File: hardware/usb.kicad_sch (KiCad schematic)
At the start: 35 parts, among them J1 USB_A_Stacked, J2 USB_C_Receptacle_USB2.0_14P, J3 USB_C_Receptacle_USB2.0_14P, J4 USB_C_Receptacle_USB2.0_14P, U10 SY6280AAC, U11 SY6280AAC, U12 SY6280AAC, U13 TPD2EUSB30, U14 TPD2EUSB30, U15 TPD2EUSB30, U16 TPD2EUSB30, U17 HUSB237, U18 TPD2EUSB30, U9 SY6280AAC

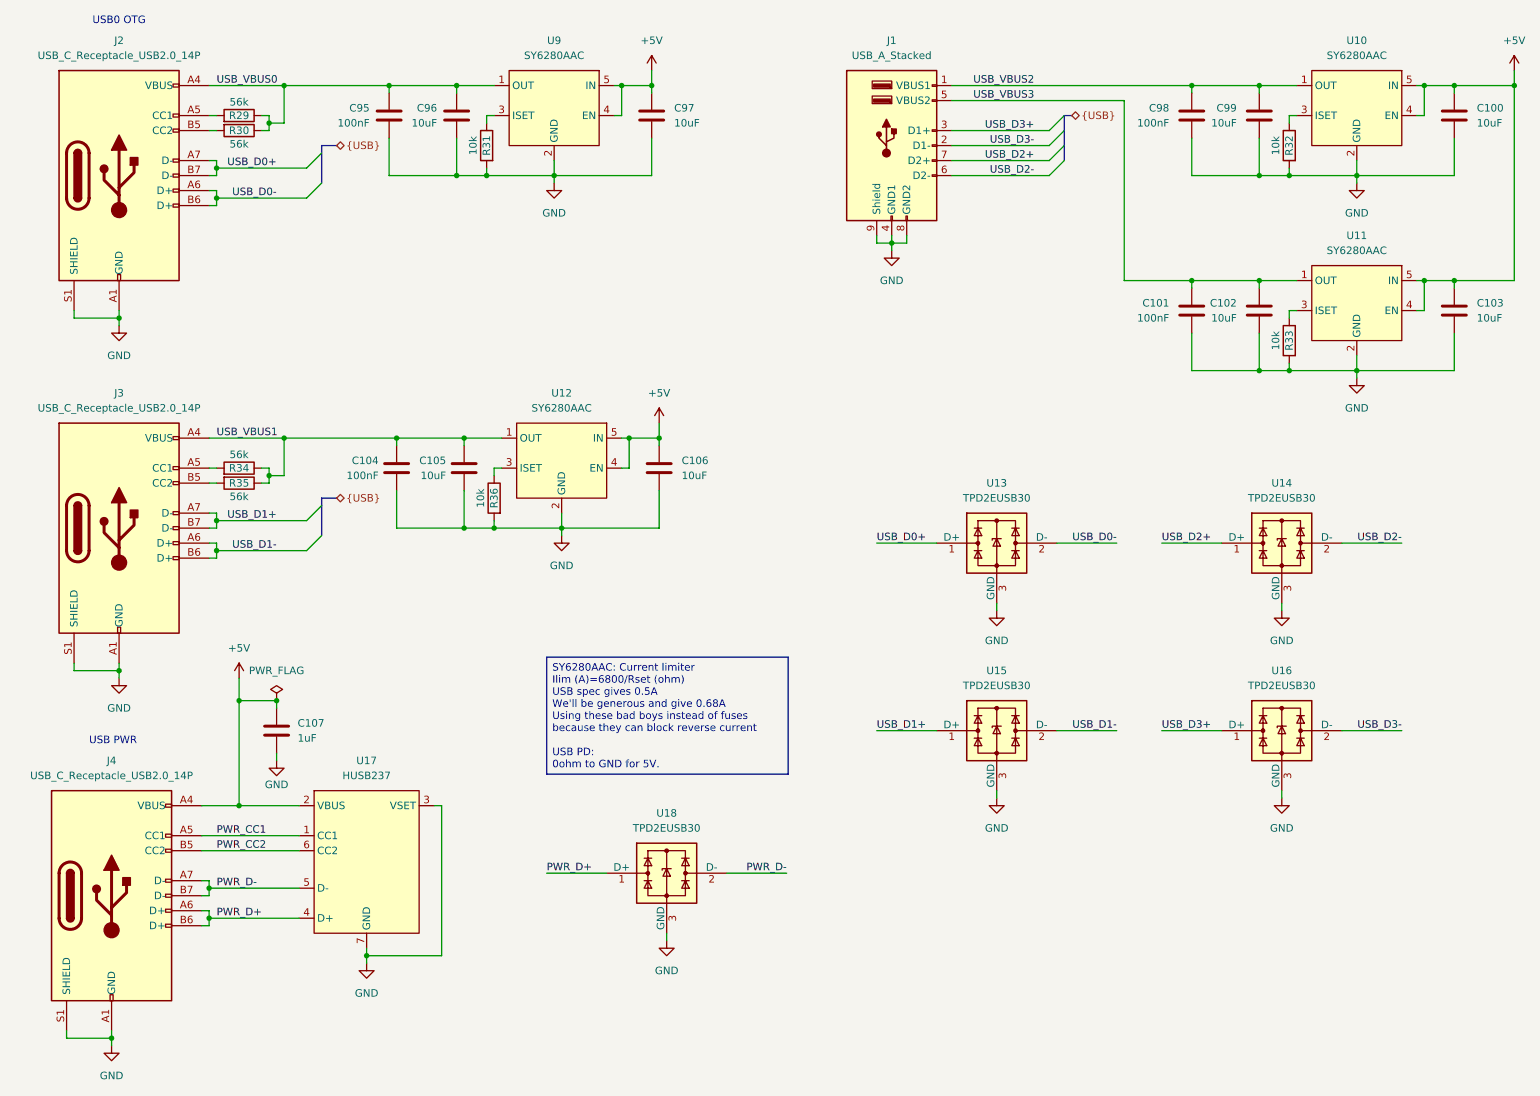
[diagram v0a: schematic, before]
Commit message: Update crystal
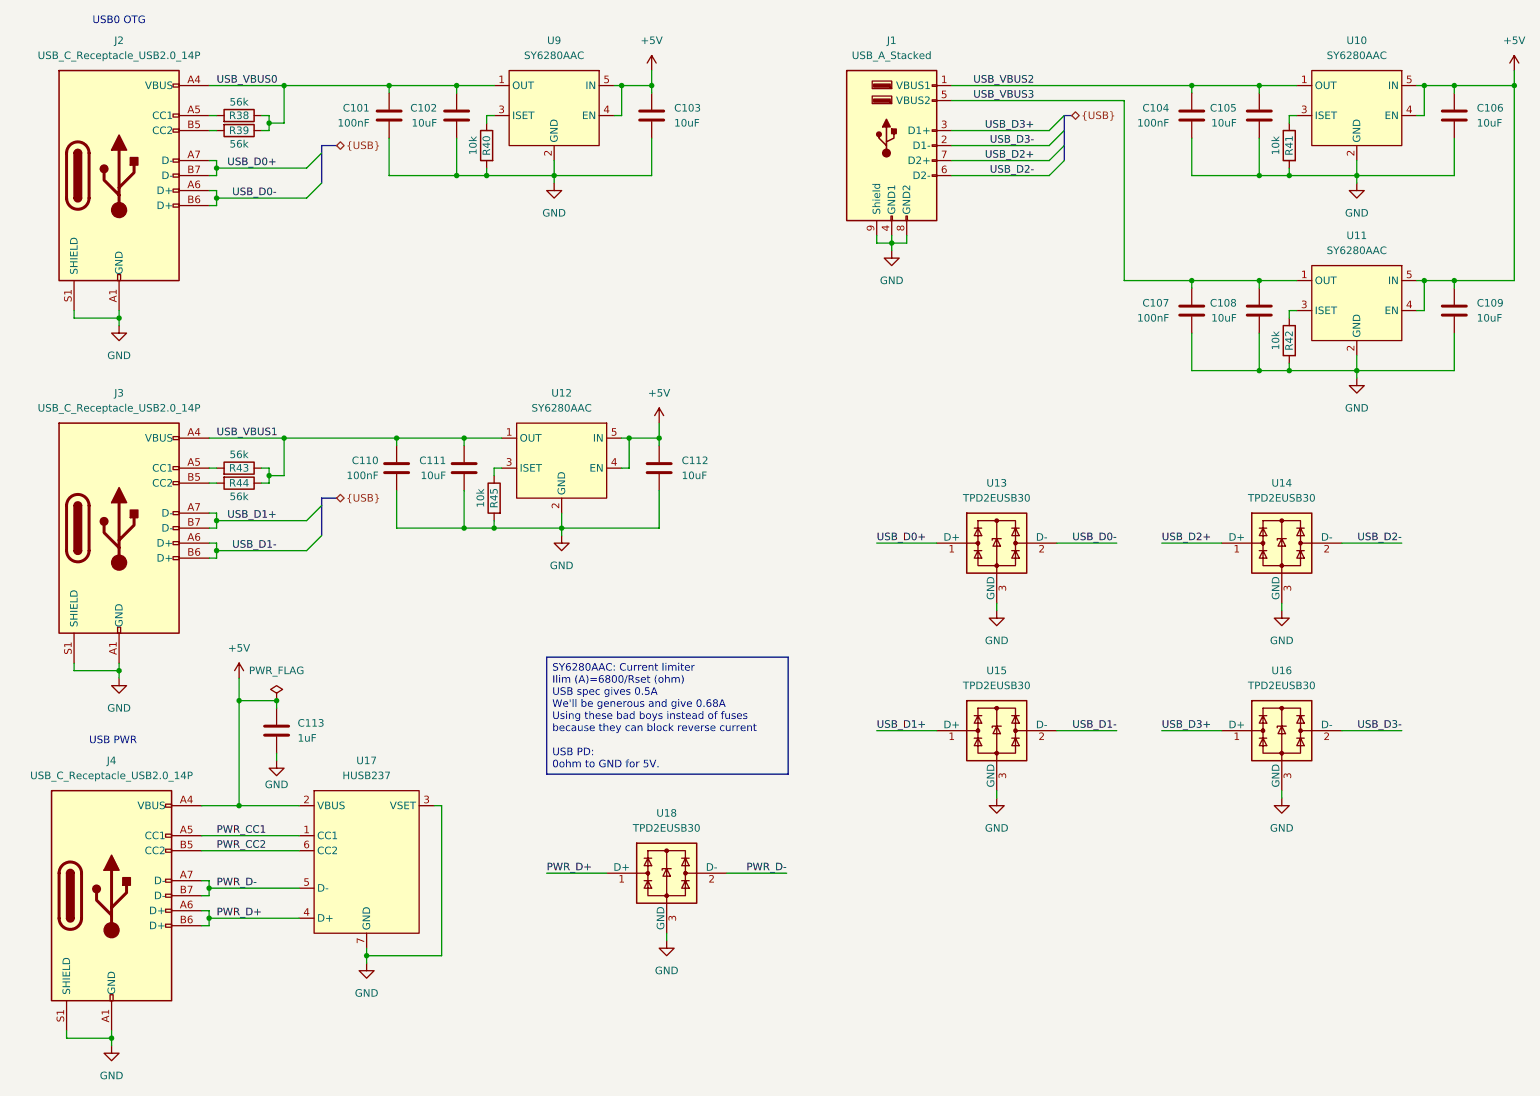
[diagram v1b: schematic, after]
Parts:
- renumbered C95 to C101, C96 to C102, C97 to C103, C98 to C104, C99 to C105, C100 to C106, C101 to C107, C102 to C108, C103 to C109, C104 to C110, C105 to C111, C106 to C112, C107 to C113, R29 to R38, R30 to R39, R31 to R40, R32 to R41, R33 to R42, R34 to R43, R35 to R44, R36 to R45

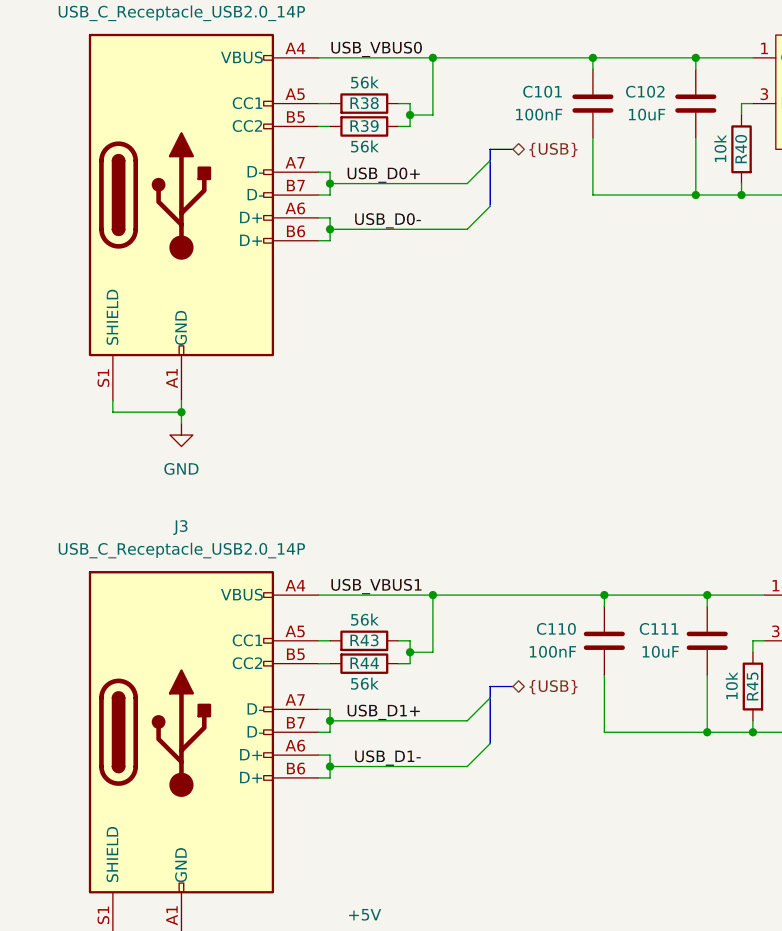
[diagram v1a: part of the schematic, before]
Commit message: Changed crystal and fix USB data lines
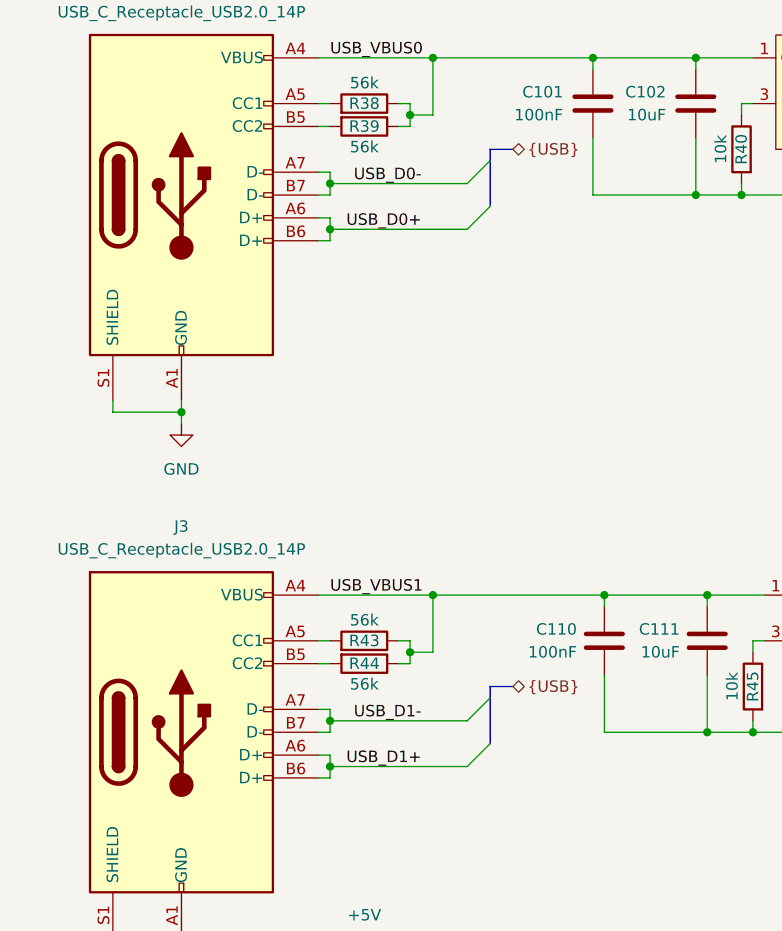
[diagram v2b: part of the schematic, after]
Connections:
- net USB_D0+: now also J2.A6 (D+), J2.B6 (D+); no longer J2.A7 (D-), J2.B7 (D-)
- net USB_D0-: now also J2.A7 (D-), J2.B7 (D-); no longer J2.A6 (D+), J2.B6 (D+)
- net USB_D1+: now also J3.A6 (D+), J3.B6 (D+); no longer J3.A7 (D-), J3.B7 (D-)
- net USB_D1-: now also J3.A7 (D-), J3.B7 (D-); no longer J3.A6 (D+), J3.B6 (D+)
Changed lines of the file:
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@@
 	)
 	(label "USB_D0-"
-		(at 72.39 45.72 180)
+		(at 72.39 40.64 180)
 		(effects
 			(font
@@
 	)
 	(label "USB_D1-"
-		(at 72.39 105.41 180)
+		(at 72.39 100.33 180)
 		(effects
 			(font
@@
 	)
 	(label "USB_D1+"
-		(at 72.39 100.33 180)
+		(at 72.39 105.41 180)
 		(effects
 			(font
@@
 	)
 	(label "USB_D0+"
-		(at 72.39 40.64 180)
+		(at 72.39 45.72 180)
 		(effects
 			(font

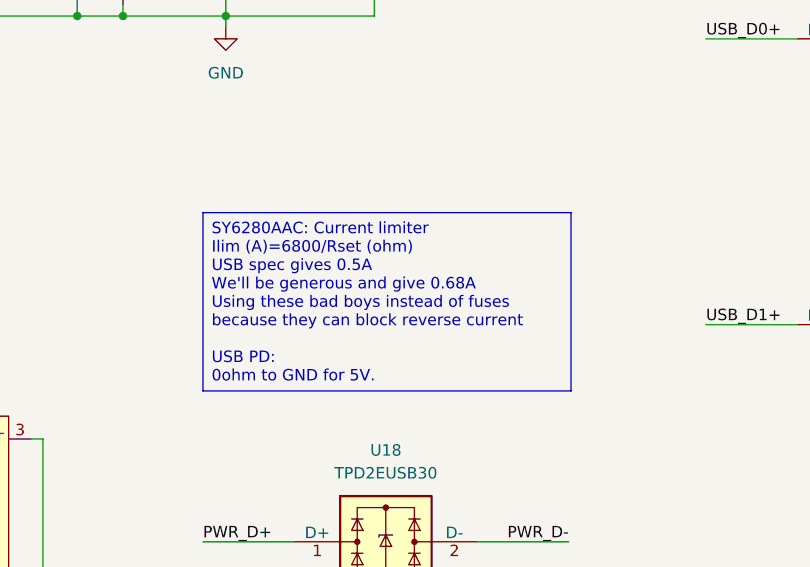
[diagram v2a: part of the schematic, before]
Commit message: Add schematic pdf
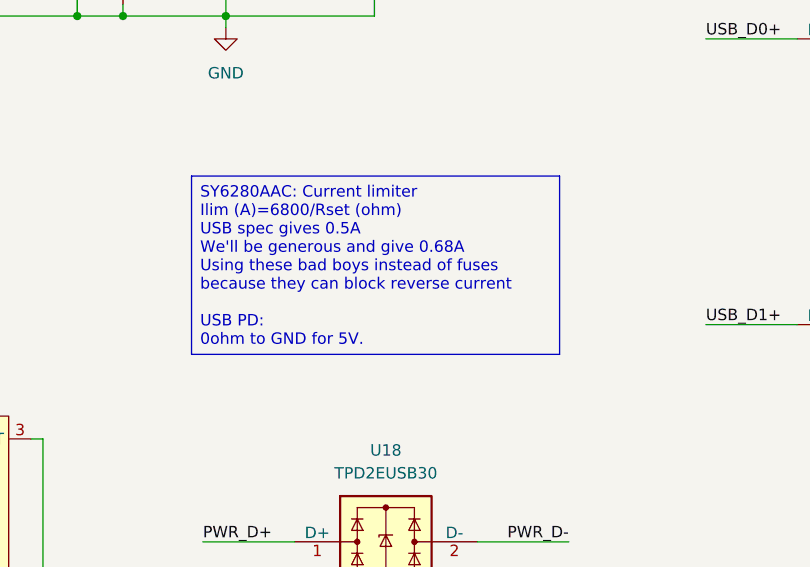
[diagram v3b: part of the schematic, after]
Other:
- title: Icepi CM0 -> Icepi SBC
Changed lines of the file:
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@@
 	(paper "A4")
 	(title_block
-		(title "Icepi CM0")
-		(date "2025-11-21")
+		(title "Icepi SBC")
+		(date "2025-12-21")
 		(rev "v1.0")
 		(company "Icy Electronics")
 		(comment 1 "Chengyin Yao (cheyao)")
-		(comment 2 "https://github.com/cheyao/icepi-cm0")
+		(comment 2 "https://github.com/cheyao/icepi-sbc")
 		(comment 3 "License: Solderpad")
 	)
@@
 	(text_box "SY6280AAC: Current limiter\nIlim (A)=6800/Rset (ohm)\nUSB spec gives 0.5A\nWe'll be generous and give 0.68A\nUsing these bad boys instead of fuses\nbecause they can block reverse current\n\nUSB PD:\n0ohm to GND for 5V."
 		(exclude_from_sim no)
-		(at 118.11 123.444 0)
+		(at 116.84 119.38 0)
 		(size 40.894 19.812)
 		(margins 0.9525 0.9525 0.9525 0.9525)
